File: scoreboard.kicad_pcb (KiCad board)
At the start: 2 copper layers, 100 x 94 mm, 95 parts, among them J101 6V In, J102 I2C, J104 Tag Connect, J105 CONN_01X02, J106 CONN_01X02, J107 CONN_01X02, J108 CONN_01X02, J109 CONN_01X02, J110 CONN_01X02, J111 CONN_01X02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

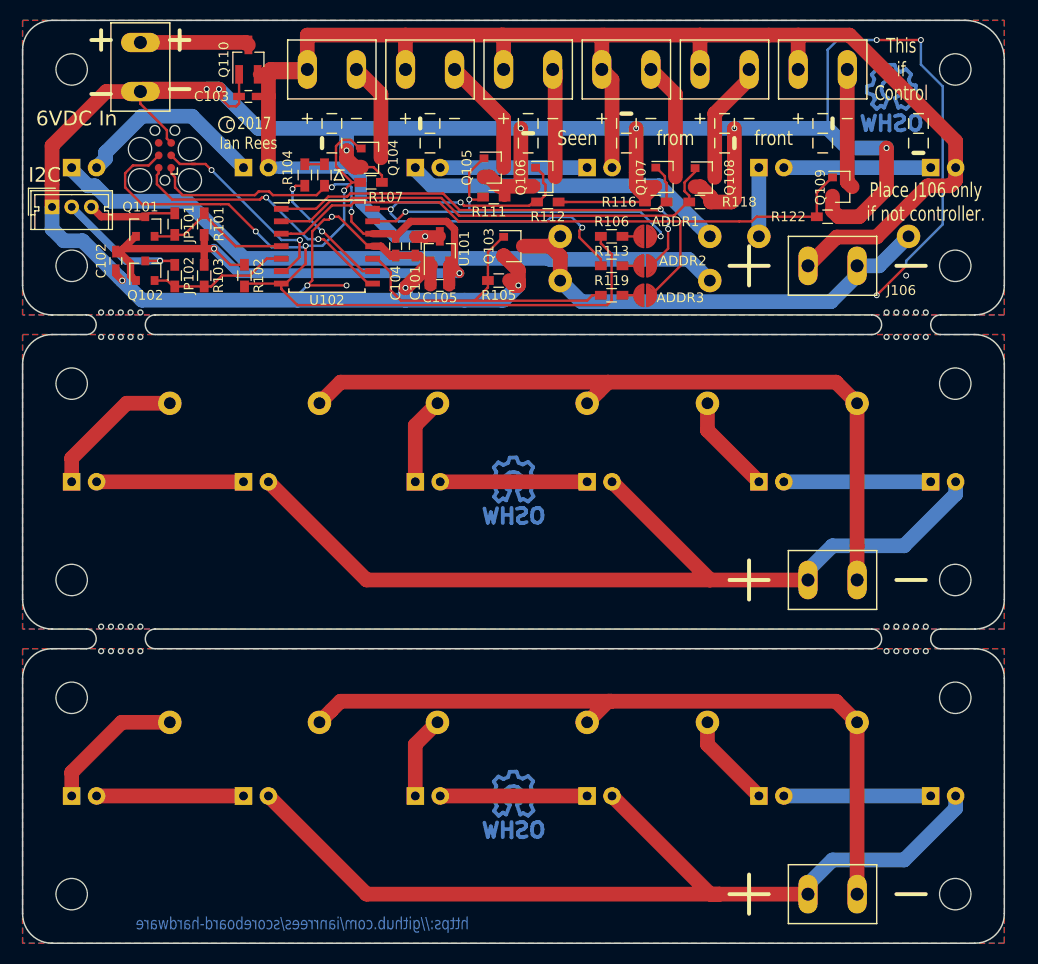
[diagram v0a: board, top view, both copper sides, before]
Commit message: PCB updated and gerbers added as ordered
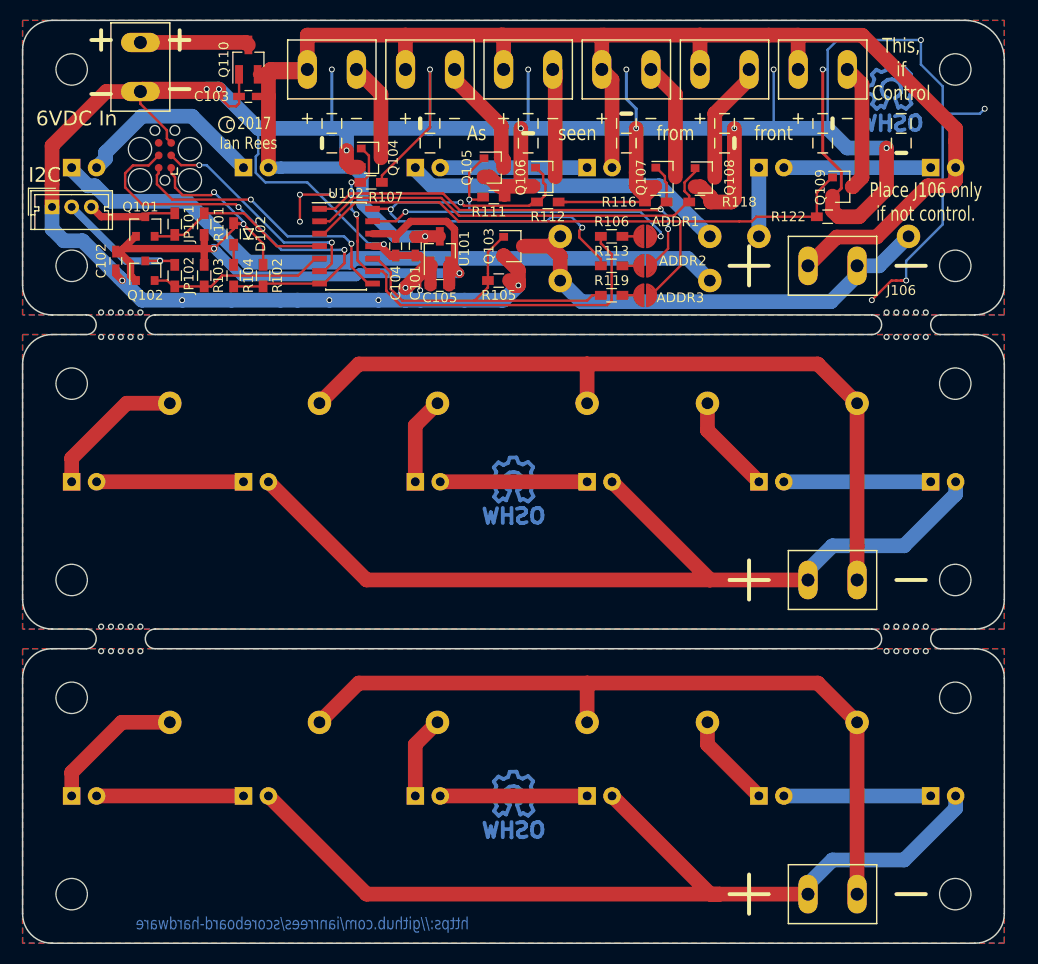
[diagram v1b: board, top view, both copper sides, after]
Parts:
- R104: value 68 -> 220
- U102: footprint soic-14w:SOIC-14W_7.5x10.3mm_Pitch1.27mm -> Housings_SOIC:SOIC-14_3.9x8.7mm_Pitch1.27mm
- moved R104 12.6 mm to (91.5, 77.0)
- moved D102 11.0 mm to (91.5, 72.8), turned to 90 degrees
- moved U102 1.95 mm to (103.0, 74.0)
- moved R102 1.90 mm to (94.5, 77.0)
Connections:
- Q104 pad 1: /SWCLK -> Net-(Q104-Pad1)
- R104 pad 2: Net-(R104-Pad2) -> /SWCLK
- R106 pad 2: /SWCLK -> Net-(Q104-Pad1)
- R107 pad 1: /SWCLK -> Net-(Q104-Pad1)
- U102 pad 9: Net-(R104-Pad2) -> Net-(Q104-Pad1)
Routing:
- net GND: track 324.8 -> 405.1 mm, vias 15 -> 28
- net /SWCLK: track 95.9 -> 44.2 mm, vias 3 -> 2
- net Net-(Q104-Pad1): track 0.00 -> 50.3 mm, vias 0 -> 2
- net Net-(R104-Pad2): track 13.8 -> 0.00 mm, vias 2 -> 0
- net +3V3: track 95.3 -> 84.3 mm
- net /TX: track 48.8 -> 44.4 mm
- net (no net): track 4.24 -> 0.00 mm, vias 2 -> 0
- net /SDA: track 15.2 -> 19.2 mm
- net /SCL: track 14.4 -> 18.3 mm
- net Net-(ADDR2-Pad2): track 52.2 -> 48.3 mm
- net /RX: track 70.3 -> 66.4 mm
- net Net-(J113-Pad2): track 77.6 -> 80.1 mm
- net Net-(J104-Pad3): track 21.3 -> 23.7 mm
- net Net-(J110-Pad2): track 77.4 -> 79.6 mm
- net /SWDIO: track 28.1 -> 29.3 mm
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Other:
- board text added: "As"
- board text added: "Place J106 only if not control."
- board text added: "This, if Control"
- board text added: "seen"
- board text removed: "Place J106 only if not controller."
- board text removed: "Seen"
- board text removed: "This if Control"
